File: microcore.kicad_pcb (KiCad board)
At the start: 4 copper layers, 90 x 76.6 mm, 33 parts, among them J1 TE_776231-1, J8 USB_B_Mini, M1 Module:mega-mcu100/0.3, M2 Module-power_12and5V-0.3, M3 Module-vr-max9924-0.3, Q1 VND14NV04-E, Q2 VND14NV04-E, Q3 VND14NV04-E, Q4 VND14NV04-E, Q5 VND14NV04-E, Q6 VND14NV04-E, Q7 VND14NV04-E

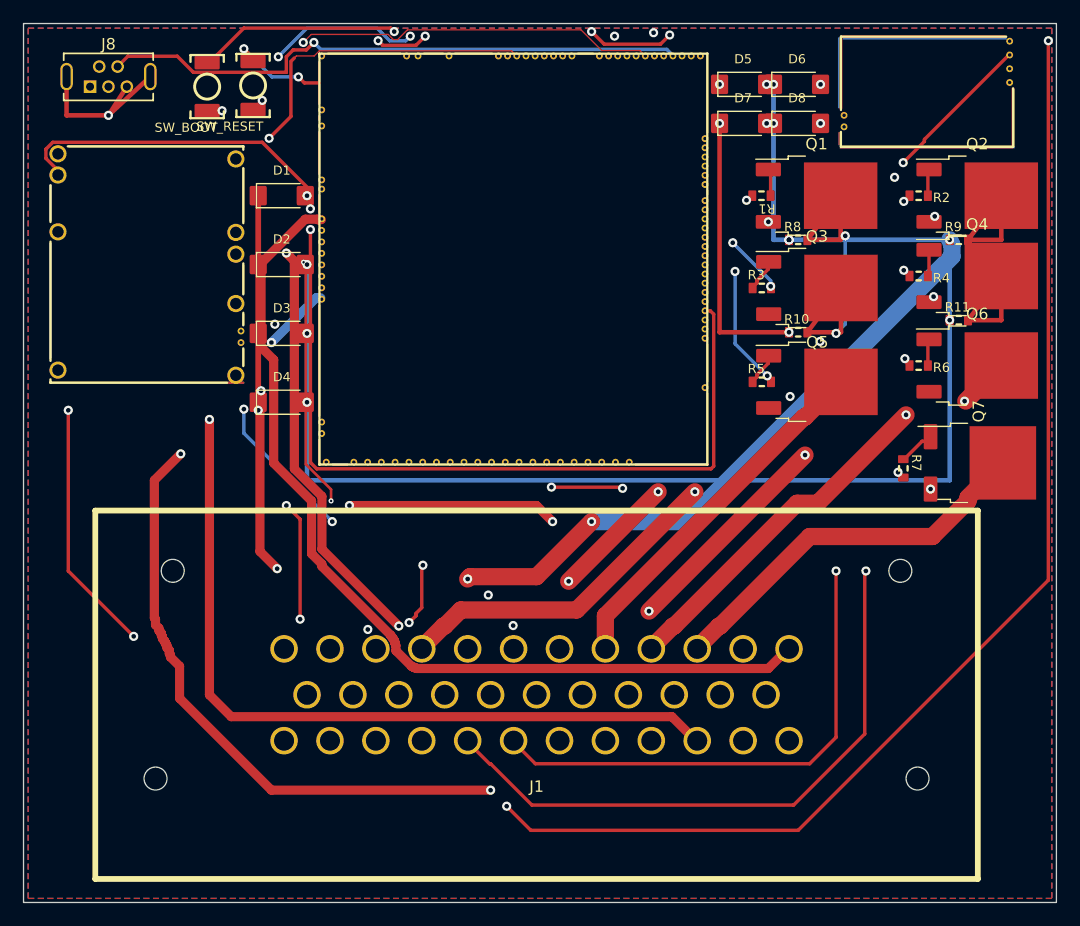
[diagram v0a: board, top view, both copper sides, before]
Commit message: Rev k: move injector diodes to B.Cu near J1; drop frame buttons
Flip D1-D4 (US1M) and D5-D8 (SMAJ33A) onto the bottom copper on the
west/east flanks of AMPSEAL J1, outside the TE_776231 silk/body keepout,
and delete the old F.Cu alley/pocket-C footprints and 0.4 mm wrap tracks.
Remove frame SW_BOOT/SW_RESET from schematic and PCB (mega-mcu100
internal buttons stay). Bump BOARD_REVISION j to k; PCB stays substantial
with Edge.Cuts drill origin unchanged.

Co-authored-by: Quintin <quintinbannink42@users.noreply.github.com>
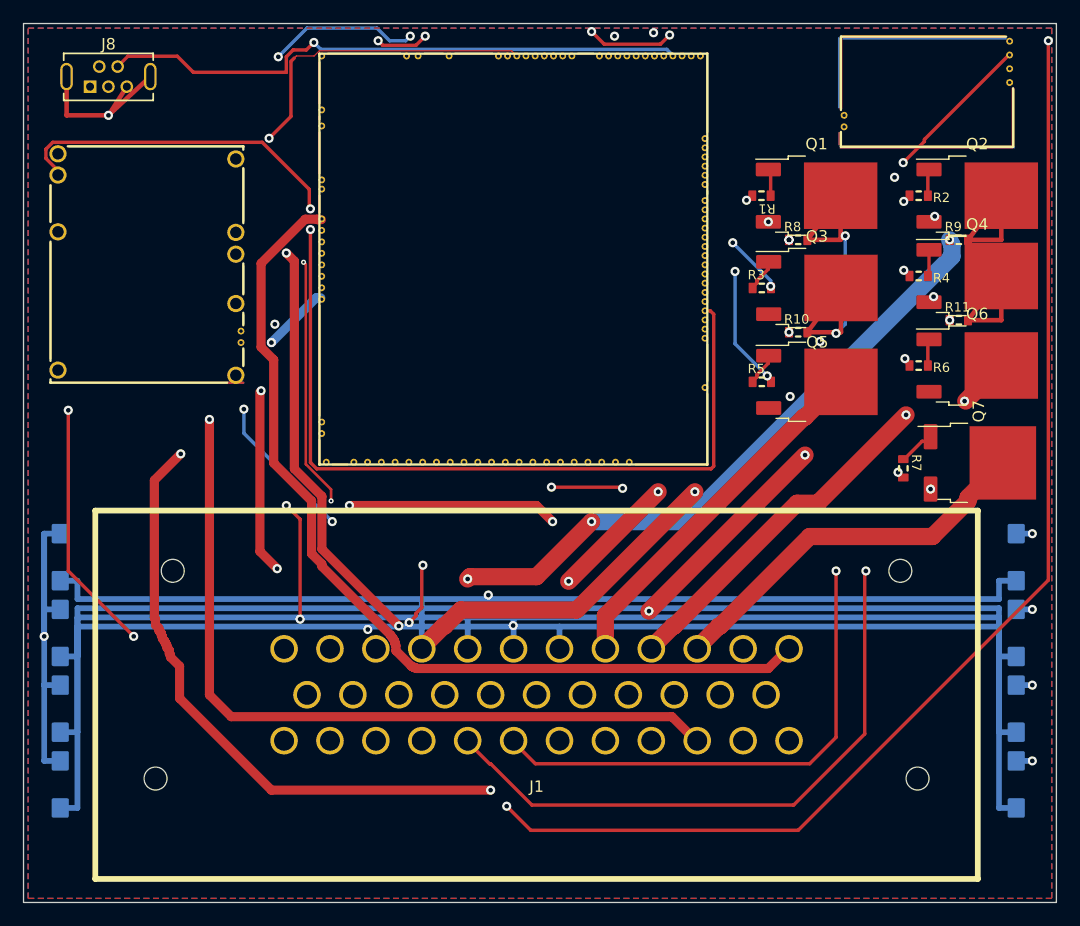
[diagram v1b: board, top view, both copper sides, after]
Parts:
- removed SW_BOOT, SW_RESET: BTN, hellen-one-common:SMD-2_2.9x3.9x1.7
- D1, D2, D3, D4, D5, D6, D7, D8: moved to B.Cu
- moved D8 60.7 mm to (194.0, 137.8), turned to 270 degrees
- moved D7 56.3 mm to (194.0, 131.2), turned to 270 degrees
- moved D6 51.5 mm to (194.0, 124.6), turned to 270 degrees
- moved D5 47.6 mm to (194.0, 118.0), turned to 270 degrees
- moved D4 38.5 mm to (110.7, 137.8), turned to 90 degrees
- moved D3 38.0 mm to (110.7, 131.2), turned to 90 degrees
- moved D2 37.5 mm to (110.7, 124.6), turned to 90 degrees
- moved D1 36.9 mm to (110.7, 118.0), turned to 90 degrees
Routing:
- net /nReset: track 39.2 -> 0.00 mm, vias 2 -> 0
- net /BOOT0: track 30.3 -> 0.00 mm, vias 1 -> 0
- net /INJ2: track 186.2 -> 156.7 mm, vias 5 -> 3
- net /V33: track 19.6 -> 0.00 mm, vias 1 -> 0
- net /INJ1: track 160.6 -> 145.4 mm, vias 5 -> 3
- net /INJ3: track 136.7 -> 149.2 mm, vias 5 -> 3
- net /V12_RAW: track 87.8 -> 94.7 mm
- net GND: track 25.6 -> 20.6 mm, vias 11 -> 9
- net /INJ4: track 161.4 -> 166.1 mm, vias 5 -> 3
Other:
- board text added: "Micro Core rev K 90x60 4-layer mega-mcu100/0.3 + power + vr-max9924/0.3 USB Mini-B + TE 776231-1 south; INJ diodes B.Cu"
- board text removed: "Micro Core rev G 90x60 4-layer mega-mcu100/0.3 + power + vr-max9924/0.3 USB Mini-B + SW_BOOT/SW_RESET north + TE 776231-1 south"

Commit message: Rev l: refill F.Cu+B.Cu GND pours; Core EFI silkscreen
Refill outer GND zones after the rev-k diode move so fab copper is
filled (0.4 mm Edge.Cuts inset, 0.2 mm clearance, thermal 0.25/0.3).
Add ASCII Core EFI branding on F.SilkS and B.SilkS. Not production-ready:
B.Cu diode collectors still need a human copper pass.

Co-authored-by: Quintin <quintinbannink42@users.noreply.github.com>
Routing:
- net GND: track 20.6 -> 15.0 mm, vias 9 -> 5
- net /INJ4: track 166.1 -> 167.5 mm, vias 3 -> 4
- net /INJ3: track 149.2 -> 150.6 mm, vias 3 -> 4
- net /INJ1: track 145.4 -> 146.8 mm, vias 3 -> 4
- net /INJ2: track 156.7 -> 158.1 mm, vias 3 -> 4
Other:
- board text added: "Core EFI"
- board text added: "Micro Core"
- board text added: "Micro Core rev L 90x76 4-layer mega-mcu100/0.3 + power + vr-max9924/0.3 USB Mini-B + TE 776231-1 south; INJ diodes B.Cu"
- board text added: "coreefi.co.za"
- board text added: "coreefi_micro"
- board text added: "microcore"
- board text added: "rev L"
- board text removed: "Micro Core rev K 90x60 4-layer mega-mcu100/0.3 + power + vr-max9924/0.3 USB Mini-B + TE 776231-1 south; INJ diodes B.Cu"

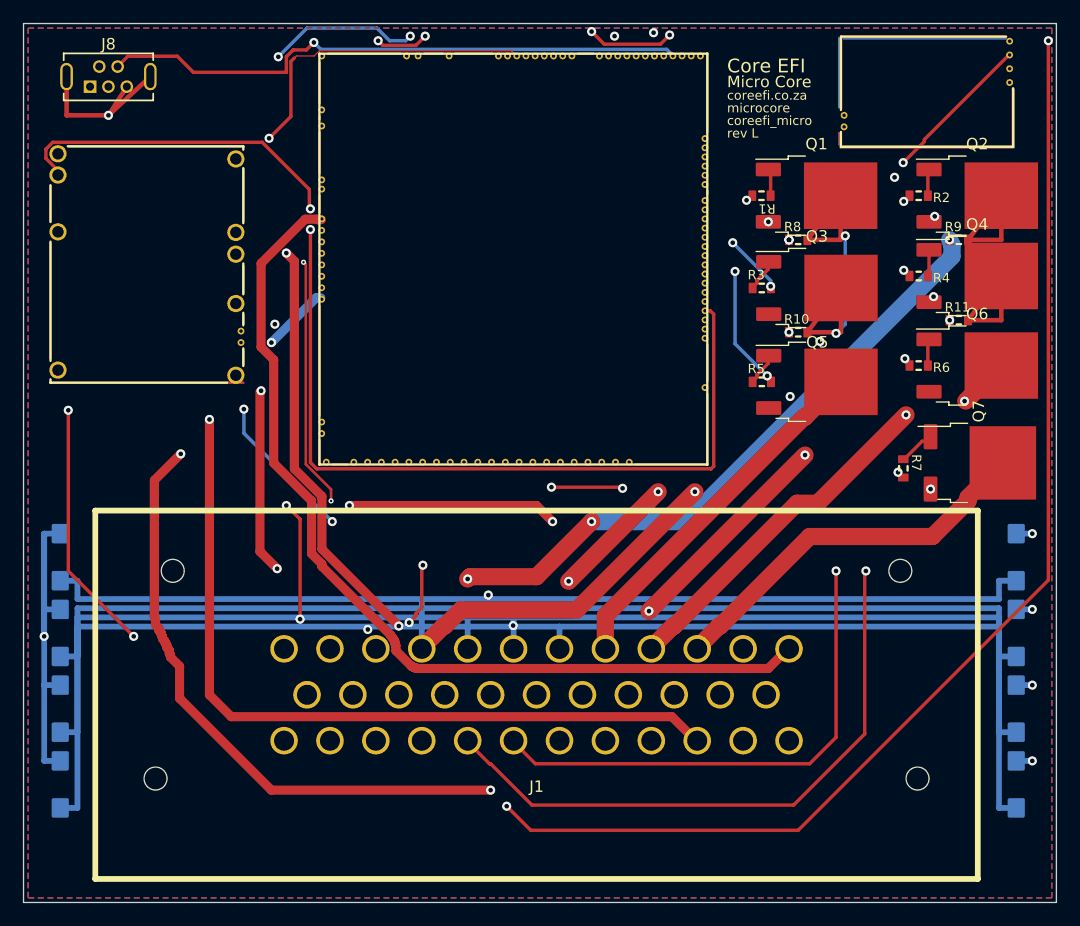
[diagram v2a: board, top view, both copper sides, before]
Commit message: Rev m: re-route D1-D8 collectors around AMPSEAL
Delete rev-k B.Cu east-west spines and opposite-pad stubs. Join
flyback/TVS pads via south-of-J1 In1/In2 buses and B.Cu GND/V12
spines on true pad Y. Refill F/B GND pours. Silk branding preserved
as rev M. Not fab-ready (Hellen keepout/padstack + leftover In1
INJ3/VR_OUT).

Co-authored-by: Quintin <quintinbannink42@users.noreply.github.com>
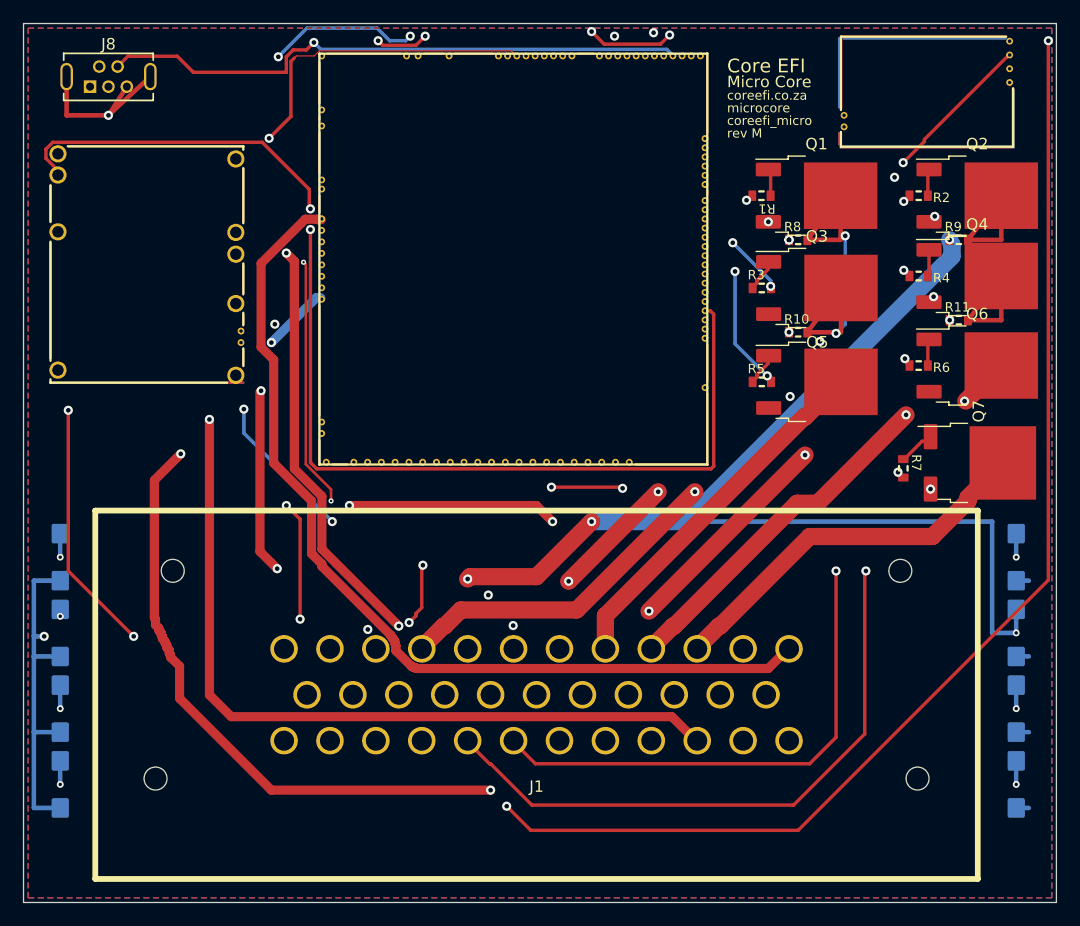
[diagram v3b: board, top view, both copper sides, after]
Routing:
- net /INJ1: track 146.8 -> 232.7 mm, vias 4 -> 5
- net /INJ2: track 158.1 -> 232.5 mm, vias 4 -> 5
- net /INJ4: track 167.5 -> 219.4 mm, vias 4 -> 5
- net /INJ3: track 150.6 -> 199.3 mm, vias 4 -> 5
- net /V12_RAW: track 94.7 -> 90.3 mm
- net GND: track 15.0 -> 19.4 mm
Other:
- board text added: "Micro Core rev M 90x76 4-layer mega-mcu100/0.3 + power + vr-max9924/0.3 USB Mini-B + TE 776231-1 south; INJ diodes B.Cu"
- board text added: "rev M"
- board text removed: "Micro Core rev L 90x76 4-layer mega-mcu100/0.3 + power + vr-max9924/0.3 USB Mini-B + TE 776231-1 south; INJ diodes B.Cu"
- board text removed: "rev L"

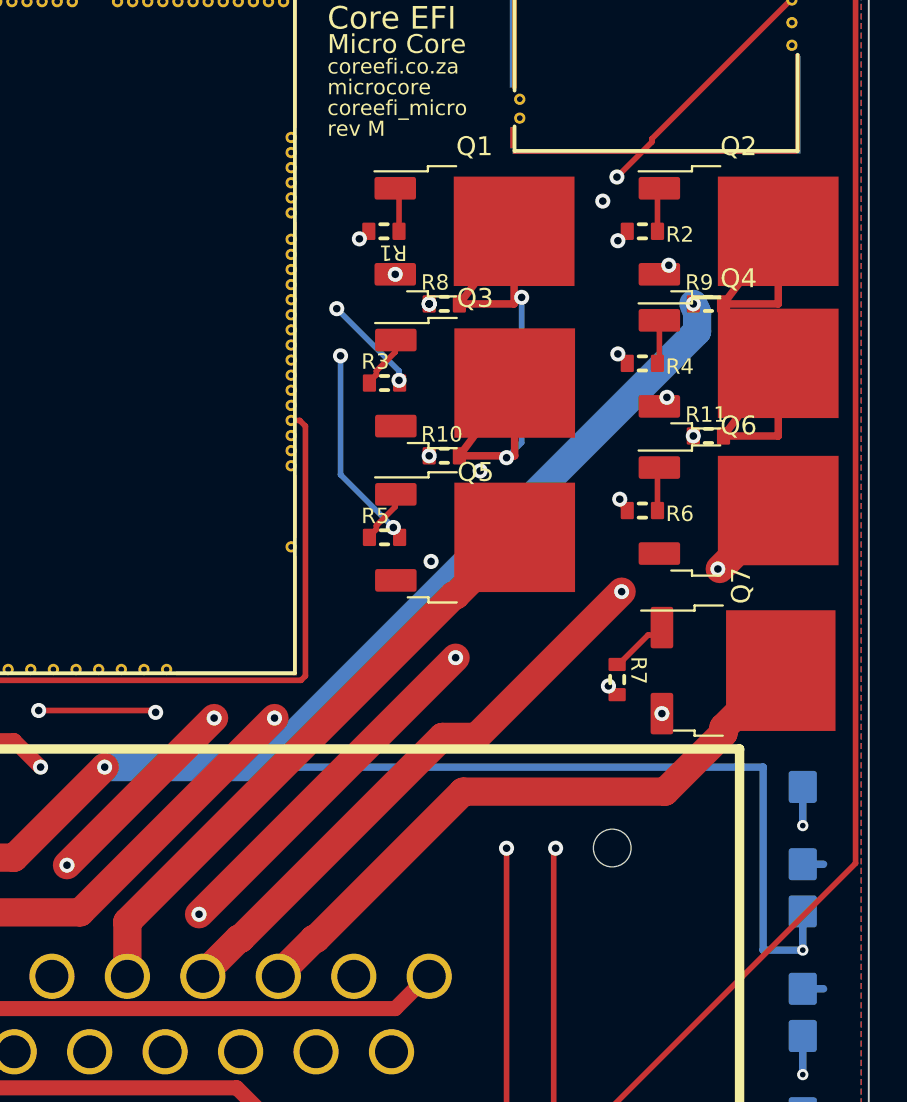
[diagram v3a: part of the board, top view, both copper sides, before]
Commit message: Rev n: F407 on mega-mcu100 and drop LS FETs
Swap module U105 from STM32F429VIT6 (C92002) to STM32F407VGT6
(LCSC C12345) in bom_replace_microcore-n.csv. Keep mega-mcu100/0.3.

Remove Q5-Q7 and gate R5-R7 from the LS3 sheet and the PCB, including
their tracks and vias. AMPSEAL pins 8/9/10 are reserved / NC.

Co-authored-by: Quintin <quintinbannink42@users.noreply.github.com>
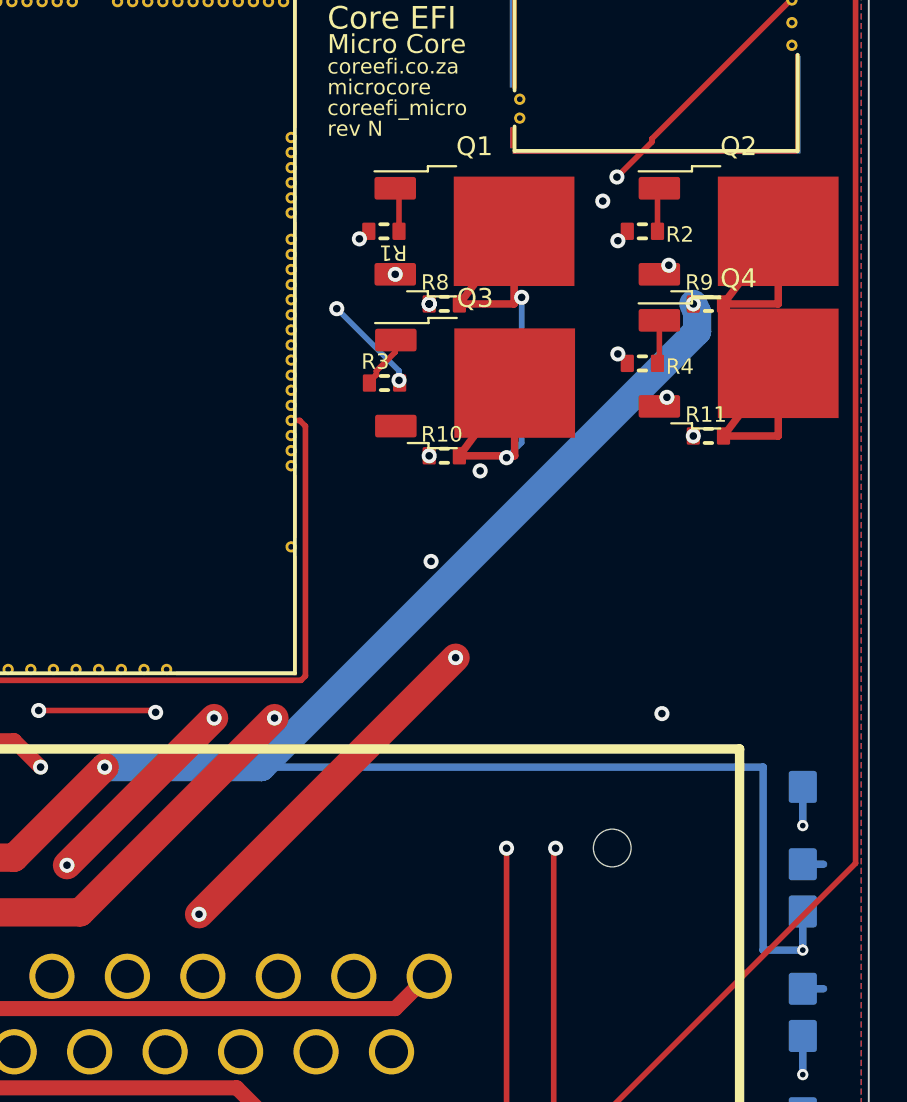
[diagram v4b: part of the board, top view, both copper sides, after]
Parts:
- removed Q5, Q6, Q7: VND14NV04-E, DPAK
- removed R5, R6, R7: 12, R0603
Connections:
- J1 pad 10: /LS3_BOOST -> (no net)
- J1 pad 8: /LS1_FP -> (no net)
- J1 pad 9: /LS2_IDLE -> (no net)
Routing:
- net /LS2_IDLE: track 40.6 -> 0.00 mm, vias 2 -> 0
- net /OUT_LS3: track 38.6 -> 0.00 mm, vias 1 -> 0
- net /LS3_BOOST: track 33.5 -> 0.00 mm
- net /LS1_FP: track 31.4 -> 0.00 mm
- net /OUT_LS2: track 27.1 -> 0.00 mm, vias 1 -> 0
- net /OUT_LS1: track 19.7 -> 0.00 mm, vias 2 -> 0
- net Net-(Q7-IN): track 3.45 -> 0.00 mm
- net Net-(Q5-IN): track 2.97 -> 0.00 mm
- net Net-(Q6-IN): track 2.36 -> 0.00 mm
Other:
- board text added: "Micro Core rev N 90x76 4-layer mega-mcu100/0.3 F407VGT6 + power + vr-max9924/0.3 USB Mini-B + TE 776231-1 south; INJ diodes B.Cu LS Q5-Q7 unstuffed"
- board text added: "rev N"
- board text removed: "Micro Core rev M 90x76 4-layer mega-mcu100/0.3 + power + vr-max9924/0.3 USB Mini-B + TE 776231-1 south; INJ diodes B.Cu"
- board text removed: "rev M"
